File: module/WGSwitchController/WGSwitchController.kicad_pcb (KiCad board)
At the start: 2 copper layers, 52.1 x 36.8 mm, 33 parts, among them M1 ARDUINO_PRO_MINI, P1 CONN_01X04, P2 CONN_01X03, P3 CONN_01X06, Q1 MMBT3906, Q2 MMBT3904, Q3 MMBT3904, Q4 MMBT3904, U1 LM7805CT

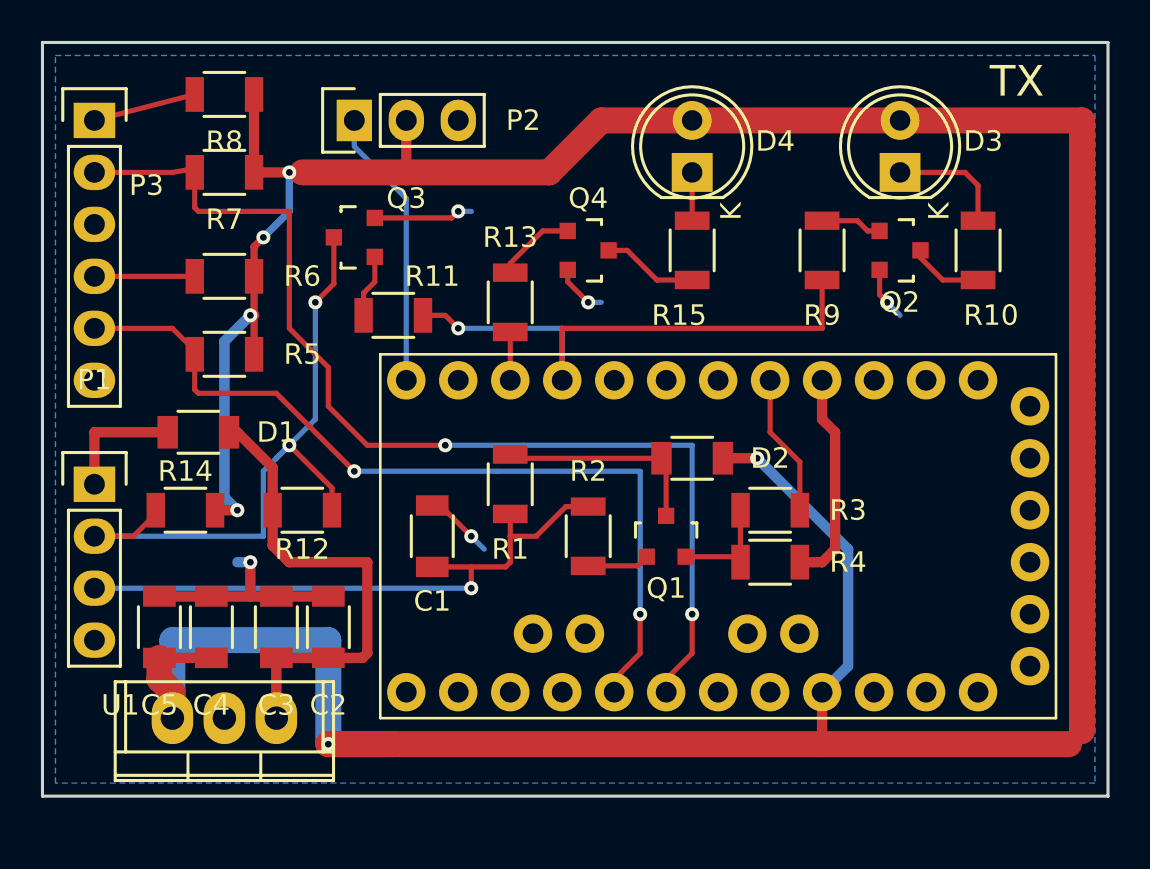
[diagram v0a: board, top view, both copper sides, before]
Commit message: Rev C of module -- fixed diode footprints.
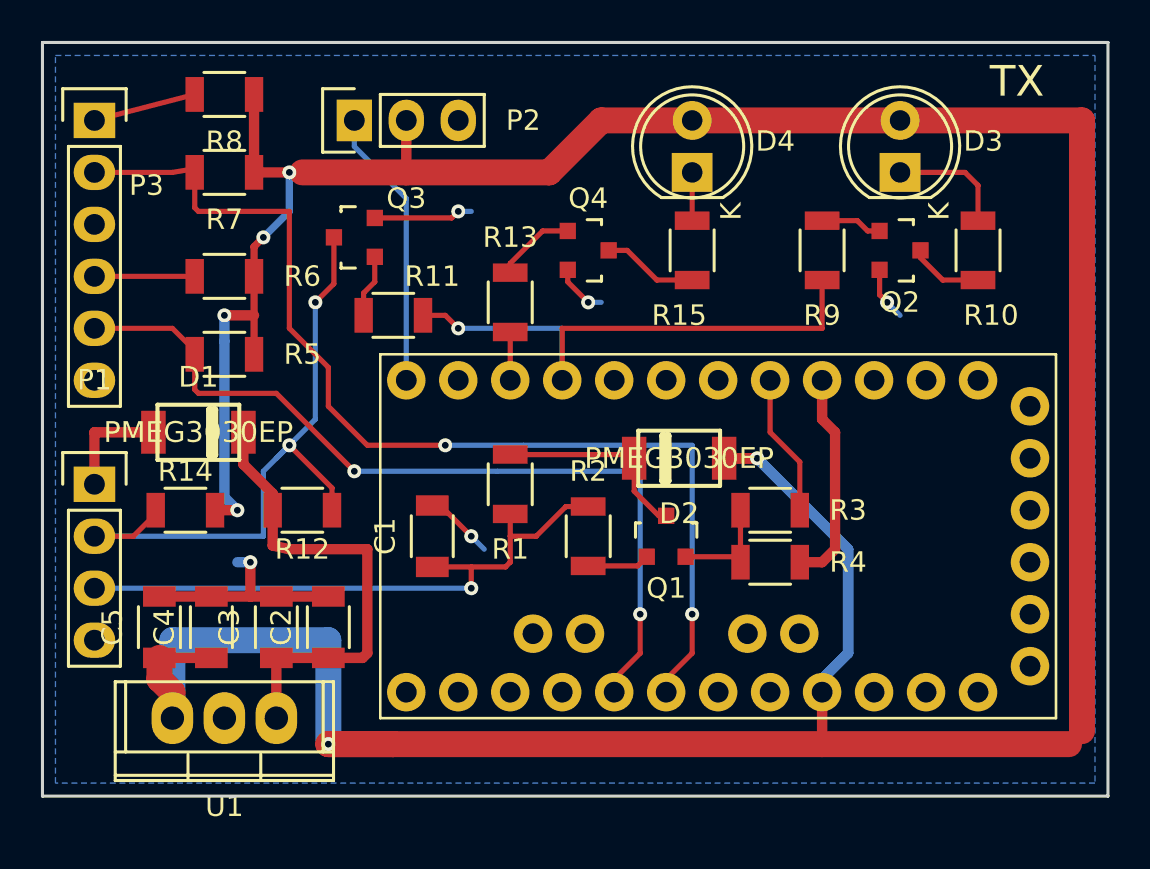
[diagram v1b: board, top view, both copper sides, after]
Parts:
- D1, D2: footprint Capacitors_SMD:C_1206 -> sod:SOD-128
- U1: footprint TO-220 -> Power_Integrations:TO-220
- moved D2 0.63 mm to (102.9, 138.4), turned to 180 degrees
- turned D1 to 0 degrees
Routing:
- net +5V: track 180.2 -> 194.6 mm
- net Net-(D1-Pad2): track 6.12 -> 5.42 mm
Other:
- board text added: "kb1vc 2017 Rev C.0"
- board text removed: "kb1vc 2017 Rev B.0"
